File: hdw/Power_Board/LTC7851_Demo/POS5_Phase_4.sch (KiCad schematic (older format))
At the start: 23 parts, among them U301 LTC7851UHH, U701 SiC779

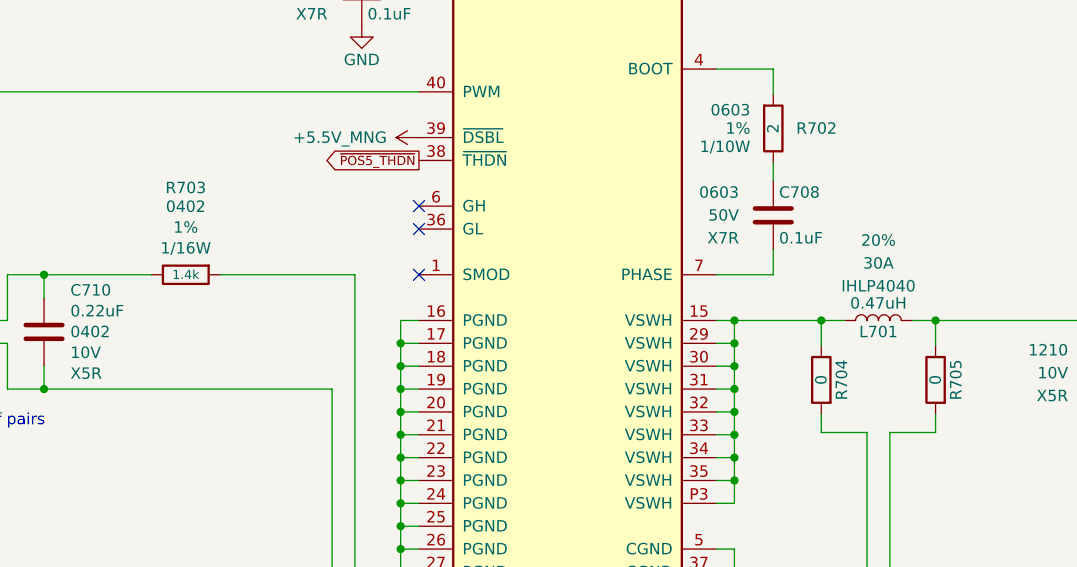
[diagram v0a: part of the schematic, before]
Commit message: Added changes to power board BOM
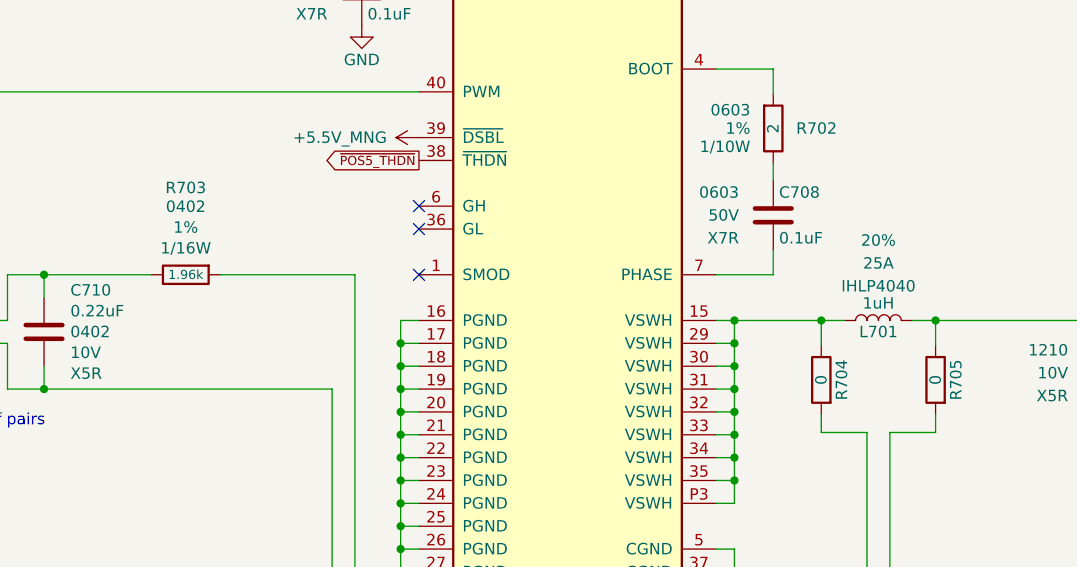
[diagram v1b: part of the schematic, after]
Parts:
- L701: value 0.47uH -> 1uH; Ampacity 30A -> 25A; Digi-Key PN 541-2595-1-ND -> 541-1306-1-ND
- R703: value 1.4k -> 1.96k; Digi-Key PN RMCF0402FT1K40CT-ND -> 311-1.96KLRCT-ND
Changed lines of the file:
@@
 AR Path="/5BB86F32/5BD4BE94" Ref="L701"  Part="1"
 F 0 "L701" V 7390 3310 50  0000 C CNN
-F 1 "0.47uH" V 7515 3310 50  0000 C CNN
+F 1 "1uH" V 7515 3310 50  0000 C CNN
 F 2 "Inductors_SMD:L_Vishay_IHLP-4040" H 7440 3310 50  0001 C CNN
 F 3 "" H 7440 3310 50  0001 C CNN
-F 4 "541-2595-1-ND" H 7440 3310 50  0001 C CNN "Digi-Key PN"
+F 4 "541-1306-1-ND" H 7440 3310 50  0001 C CNN "Digi-Key PN"
 F 5 "IHLP4040" V 7590 3310 50  0000 C CNN "display_footprint"
-F 6 "30A" V 7690 3310 50  0000 C CNN "Ampacity"
+F 6 "25A" V 7690 3310 50  0000 C CNN "Ampacity"
 F 7 "20%" V 7790 3310 50  0000 C CNN "Tolerance"
 	1    7440 3310
@@
 AR Path="/5BB86F32/5BE7E56E" Ref="R703"  Part="1"
 F 0 "R703" V 4790 3110 50  0000 C CNN
-F 1 "1.4k" V 4410 3110 40  0000 C CNN
+F 1 "1.96k" V 4410 3110 40  0000 C CNN
 F 2 "Resistors_SMD:R_0402" H 4410 3110 50  0001 C CNN
 F 3 "" H 4410 3110 50  0001 C CNN
-F 4 "RMCF0402FT1K40CT-ND" H 4710 3510 60  0001 C CNN "Digi-Key PN"
+F 4 "311-1.96KLRCT-ND" H 4710 3510 60  0001 C CNN "Digi-Key PN"
 F 5 "0402" V 4708 3110 50  0000 C CNN "display_footprint"
 F 6 "1%" V 4617 3110 50  0000 C CNN "Tolerance"

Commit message: Merging drews_branch_3 into master
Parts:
- C701, C702, C703, C705, C707, C715: symbol Custom_Library:CP_Tant_Custom -> LED_Display_Local_Library:CP_Tant_Custom
- C704, C706, C708, C709, C710, C711, C712, C713, C714: symbol Custom_Library:C_Custom -> LED_Display_Local_Library:C_Custom
- L701: symbol Custom_Library:L_Custom -> LED_Display_Local_Library:L_Custom
- R701, R702, R703, R704, R705: symbol Custom_Library:R_Custom -> LED_Display_Local_Library:R_Custom
- U301: symbol Custom_Library:LTC7851UHH -> LED_Display_Local_Library:LTC7851UHH
- U701: symbol Custom_Library:SiC779 -> LED_Display_Local_Library:SiC779
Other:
- note added: "07. +5V Phase 4"
- note removed: "+5V Phase 4"
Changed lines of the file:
@@
 POS5_PGOOD_OC
 $Comp
-L Custom_Library:C_Custom C?
+L LED_Display_Local_Library:C_Custom C?
 U 1 1 5BD4BE0C
 P 4560 1340
@@
 F 2 "Capacitors_SMD:C_0603" H 4598 1190 50  0001 C CNN
 F 3 "" H 4585 1440 50  0001 C CNN
-F 4 "0603" H 4410 1440 50  0000 R CNN "display_footprint"
-F 5 "16V" H 4410 1340 50  0000 R CNN "Voltage"
-F 6 "X7R" H 4410 1240 50  0000 R CNN "Dielectric"
-F 7 "1276-6524-1-ND" H 4985 1840 60  0001 C CNN "Digi-Key PN"
+F 4 "1276-6524-1-ND" H 4985 1840 60  0001 C CNN "Digi-Key PN"
+F 5 "0603" H 4410 1440 50  0000 R CNN "display_footprint"
+F 6 "16V" H 4410 1340 50  0000 R CNN "Voltage"
+F 7 "X7R" H 4410 1240 50  0000 R CNN "Dielectric"
 	1    4560 1340
 	1    0    0    -1
@@
 $EndComp
 $Comp
-L Custom_Library:SiC779 U?
+L LED_Display_Local_Library:SiC779 U?
 U 1 1 5BD4BE1A
 P 6080 2810
@@
 	6810 3910 6810 4010
 $Comp
-L Custom_Library:L_Custom L?
+L LED_Display_Local_Library:L_Custom L?
 U 1 1 5BD4BE94
 P 7440 3310
@@
 	6810 1710 6810 1810
 $Comp
-L Custom_Library:R_Custom R?
+L LED_Display_Local_Library:R_Custom R?
 U 1 1 5BD4BEB5
 P 6980 2470
@@
 $EndComp
 $Comp
-L Custom_Library:C_Custom C?
+L LED_Display_Local_Library:C_Custom C?
 U 1 1 5BD4BEC0
 P 6980 2850
@@
 F 2 "Capacitors_SMD:C_0603" H 7018 2700 50  0001 C CNN
 F 3 "" H 7005 2950 50  0001 C CNN
-F 4 "0603" H 6830 2950 50  0000 R CNN "display_footprint"
-F 5 "50V" H 6830 2850 50  0000 R CNN "Voltage"
-F 6 "X7R" H 6830 2750 50  0000 R CNN "Dielectric"
-F 7 "490-4779-1-ND" H 7405 3350 60  0001 C CNN "Digi-Key PN"
+F 4 "490-4779-1-ND" H 7405 3350 60  0001 C CNN "Digi-Key PN"
+F 5 "0603" H 6830 2950 50  0000 R CNN "display_footprint"
+F 6 "50V" H 6830 2850 50  0000 R CNN "Voltage"
+F 7 "X7R" H 6830 2750 50  0000 R CNN "Dielectric"
 	1    6980 2850
 	1    0    0    -1
@@
 Connection ~ 6810 3310
 $Comp
-L Custom_Library:C_Custom C?
+L LED_Display_Local_Library:C_Custom C?
 U 1 1 5BD4BEF6
 P 7880 1340
@@
 	8480 1110 7880 1110
 $Comp
-L Custom_Library:C_Custom C?
+L LED_Display_Local_Library:C_Custom C?
 U 1 1 5BD4BF1D
 P 8420 3540
@@
 F 2 "Capacitors_SMD:C_1210" H 8458 3390 50  0001 C CNN
 F 3 "" H 8445 3640 50  0001 C CNN
-F 4 "1210" H 8270 3640 50  0000 R CNN "display_footprint"
-F 5 "10V" H 8270 3540 50  0000 R CNN "Voltage"
-F 6 "X5R" H 8270 3440 50  0000 R CNN "Dielectric"
-F 7 "587-3432-1-ND" H 8845 4040 60  0001 C CNN "Digi-Key PN"
+F 4 "587-3432-1-ND" H 8845 4040 60  0001 C CNN "Digi-Key PN"
+F 5 "1210" H 8270 3640 50  0000 R CNN "display_footprint"
+F 6 "10V" H 8270 3540 50  0000 R CNN "Voltage"
+F 7 "X5R" H 8270 3440 50  0000 R CNN "Dielectric"
 	1    8420 3540
 	1    0    0    -1
@@
 $EndComp
 $Comp
-L Custom_Library:LTC7851UHH U?
+L LED_Display_Local_Library:LTC7851UHH U?
 U 5 1 5BD4BF5A
 P 2510 4210
@@
 $EndComp
 $Comp
-L Custom_Library:C_Custom C?
+L LED_Display_Local_Library:C_Custom C?
 U 1 1 5BD4BF70
 P 5180 1870
@@
 F 2 "Capacitors_SMD:C_0603" H 5218 1720 50  0001 C CNN
 F 3 "" H 5205 1970 50  0001 C CNN
-F 4 "0603" H 5030 1970 50  0000 R CNN "display_footprint"
-F 5 "50V" H 5030 1870 50  0000 R CNN "Voltage"
-F 6 "X7R" H 5030 1770 50  0000 R CNN "Dielectric"
-F 7 "490-4779-1-ND" H 5605 2370 60  0001 C CNN "Digi-Key PN"
+F 4 "490-4779-1-ND" H 5605 2370 60  0001 C CNN "Digi-Key PN"
+F 5 "0603" H 5030 1970 50  0000 R CNN "display_footprint"
+F 6 "50V" H 5030 1870 50  0000 R CNN "Voltage"
+F 7 "X7R" H 5030 1770 50  0000 R CNN "Dielectric"
 	1    5180 1870
 	1    0    0    -1
 $EndComp
 $Comp
-L Custom_Library:R_Custom R?
+L LED_Display_Local_Library:R_Custom R?
 U 1 1 5BD4BF7B
 P 5180 1340
@@
 	8480 1030 8480 1110
 $Comp
-L Custom_Library:C_Custom C?
+L LED_Display_Local_Library:C_Custom C?
 U 1 1 5BD4BF8D
 P 7280 1340
@@
 F 2 "Capacitors_SMD:C_0603" H 7318 1190 50  0001 C CNN
 F 3 "" H 7305 1440 50  0001 C CNN
-F 4 "0603" H 7130 1440 50  0000 R CNN "display_footprint"
-F 5 "16V" H 7130 1340 50  0000 R CNN "Voltage"
-F 6 "X7R" H 7130 1240 50  0000 R CNN "Dielectric"
-F 7 "1276-6524-1-ND" H 7705 1840 60  0001 C CNN "Digi-Key PN"
+F 4 "1276-6524-1-ND" H 7705 1840 60  0001 C CNN "Digi-Key PN"
+F 5 "0603" H 7130 1440 50  0000 R CNN "display_footprint"
+F 6 "16V" H 7130 1340 50  0000 R CNN "Voltage"
+F 7 "X7R" H 7130 1240 50  0000 R CNN "Dielectric"
 	1    7280 1340
 	1    0    0    -1
@@
 Connection ~ 9020 3310
 $Comp
-L Custom_Library:CP_Tant_Custom C?
+L LED_Display_Local_Library:CP_Tant_Custom C?
 U 1 1 5BD4BF99
 P 9620 3540
@@
 $EndComp
 $Comp
-L Custom_Library:C_Custom C?
+L LED_Display_Local_Library:C_Custom C?
 U 1 1 5BD4BFCC
 P 9020 3540
@@
 $EndComp
 $Comp
-L Custom_Library:C_Custom C?
+L LED_Display_Local_Library:C_Custom C?
 U 1 1 5BD4BFD8
 P 8480 1340
@@
 $EndComp
 $Comp
-L Custom_Library:CP_Tant_Custom C?
+L LED_Display_Local_Library:CP_Tant_Custom C?
 U 1 1 5BD4BFE3
 P 3330 7370
@@
 $EndComp
 $Comp
-L Custom_Library:CP_Tant_Custom C?
+L LED_Display_Local_Library:CP_Tant_Custom C?
 U 1 1 5BD4BFEE
 P 3930 7370
@@
 $EndComp
 $Comp
-L Custom_Library:CP_Tant_Custom C?
+L LED_Display_Local_Library:CP_Tant_Custom C?
 U 1 1 5BD4BFF9
 P 4530 7370
@@
 $EndComp
 $Comp
-L Custom_Library:CP_Tant_Custom C?
+L LED_Display_Local_Library:CP_Tant_Custom C?
 U 1 1 5BD4C004
 P 5130 7370
@@
 $EndComp
 $Comp
-L Custom_Library:CP_Tant_Custom C?
+L LED_Display_Local_Library:CP_Tant_Custom C?
 U 1 1 5BD4C00F
 P 5730 7370
@@
 Connection ~ 6810 4010
 Text Notes 540  690  0    100  ~ 20
-+5V Phase 4
+07. +5V Phase 4
 NoConn ~ 5430 2810
 NoConn ~ 5430 2910
@@
 $EndComp
 $Comp
-L Custom_Library:R_Custom R?
+L LED_Display_Local_Library:R_Custom R?
 U 1 1 5BE7E56E
 P 4410 3110
@@
 $EndComp
 $Comp
-L Custom_Library:C_Custom C?
+L LED_Display_Local_Library:C_Custom C?
 U 1 1 5BE7E579
 P 3790 3360
@@
 	7190 3310 7190 3420
 $Comp
-L Custom_Library:R_Custom R?
+L LED_Display_Local_Library:R_Custom R?
 U 1 1 5BE7E599
 P 7190 3570
@@
 $EndComp
 $Comp
-L Custom_Library:R_Custom R?
+L LED_Display_Local_Library:R_Custom R?
 U 1 1 5BE7E5A4
 P 7690 3570
@@
 Wire Wire Line
 	7690 3310 8420 3310
+$Comp
+L LED_Display_Local_Library:MU_Logo #G?
+U 1 1 5C003DBA
+P 9900 1100
+F 0 "#G?" H 9900 614 60  0001 C CNN
+F 1 "MU_Logo" H 9900 1586 60  0001 C CNN
+F 2 "" H 9900 1100 50  0001 C CNN
+F 3 "" H 9900 1100 50  0001 C CNN
+	1    9900 1100
+	1    0    0    -1
+$EndComp
 $EndSCHEMATC

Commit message: Schematic cleanup
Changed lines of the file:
@@
 Date "2018-11-28"
 Rev "A"
-Comp "Marquette Senior Design 2018, Group E44"
+Comp "Marquette University Senior Design 2018 Group E44"
 Comment1 ""
 Comment2 ""
@@
 AR Path="/5BB86F2C/5BD4BEB5" Ref="R?"  Part="1"
 AR Path="/5BB86F32/5BD4BEB5" Ref="R702"  Part="1"
-F 0 "R702" H 6880 2470 50  0000 R CNN
+F 0 "R702" H 6920 2470 50  0000 R CNN
 F 1 "2" V 6980 2470 50  0000 C CNN
 F 2 "Resistors_SMD:R_0603" H 6980 2470 50  0001 C CNN
@@
 AR Path="/5BB86F2C/5BD4BF7B" Ref="R?"  Part="1"
 AR Path="/5BB86F32/5BD4BF7B" Ref="R701"  Part="1"
-F 0 "R701" H 5080 1340 50  0000 R CNN
+F 0 "R701" H 5120 1340 50  0000 R CNN
 F 1 "2" V 5180 1340 50  0000 C CNN
 F 2 "Resistors_SMD:R_0603" H 5180 1340 50  0001 C CNN
@@
 AR Path="/5BB86F29/5BE7E599" Ref="R?"  Part="1"
 AR Path="/5BB86F32/5BE7E599" Ref="R704"  Part="1"
-F 0 "R704" V 7280 3570 50  0000 C CNN
+F 0 "R704" H 7240 3570 50  0000 L CNN
 F 1 "0" V 7190 3570 50  0000 C CNN
 F 2 "Resistors_SMD:R_0402" H 7190 3570 50  0001 C CNN
@@
 AR Path="/5BB86F29/5BE7E5A4" Ref="R?"  Part="1"
 AR Path="/5BB86F32/5BE7E5A4" Ref="R705"  Part="1"
-F 0 "R705" V 7780 3570 50  0000 C CNN
+F 0 "R705" H 7740 3570 50  0000 L CNN
 F 1 "0" V 7690 3570 50  0000 C CNN
 F 2 "Resistors_SMD:R_0402" H 7690 3570 50  0001 C CNN
